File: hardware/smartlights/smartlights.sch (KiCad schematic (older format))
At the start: 9 parts, among them J1 Conn_02x20_Odd_Even_MountingP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, J2 Conn_01x02_MountingPin, J3 Conn_Coaxial_Power, Q1 IRLZ34N, U1 LM2596T-5

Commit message: Add switches to PCB, enlarging it.
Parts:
- added J10, J11, J4, J6, J7, J8, J9: Conn_01x02_MountingPin, Connector_PinHeader_2.54mm:PinHeader_1x02_P2.54mm_Vertical, symbol Connector_Generic:Conn_01x02
- added J5: Conn_01x04, Connector_PinHeader_2.54mm:PinHeader_1x04_P2.54mm_Vertical, symbol Connector_Generic:Conn_01x04
- added Q2, Q3, Q4, Q5, Q6: IRLZ34N, Package_TO_SOT_THT:TO-220-3_Vertical, symbol Transistor_FET:IRLZ34N
- J1: symbol Connector_Generic_MountingPin:Conn_02x20_Odd_Even_MountingPin -> Connector_Generic:Conn_02x20_Odd_Even
- J2: symbol Connector_Generic_MountingPin:Conn_01x02_MountingPin -> Connector_Generic:Conn_01x02
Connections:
- net labels added: 12V, 5V, 5V_raw, Data_19, Data_21, Data_7, Data_B, Data_G, Data_R, PWR,21, PWR_19, PWR_7, PWR_B, PWR_G, PWR_R
- wire segments 43 -> 70
- no-connect marks 39 -> 27
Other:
- moved on the sheet: C1, C2, D1, J3, L1, Q1, U1

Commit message: Neaten up labels, GND area
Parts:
- renumbered J2 to J1, J3 to J10, J1 to J11, J5 to J2, J6 to J3, J9 to J5, J8 to J6, J11 to J8, J10 to J9
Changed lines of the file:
@@
 $EndComp
 $Comp
-L Connector_Generic:Conn_01x04 J5
+L Connector_Generic:Conn_01x04 J2
 U 1 1 5E66A677
 P 900 4250
-F 0 "J5" V 864 3962 50  0000 R CNN
+F 0 "J2" V 864 3962 50  0000 R CNN
 F 1 "Conn_01x04" V 773 3962 50  0000 R CNN
 F 2 "Connector_PinHeader_2.54mm:PinHeader_1x04_P2.54mm_Vertical" H 900 4250 50  0001 C CNN
@@
 	1450 4150 1100 4150
 $Comp
-L Connector_Generic:Conn_01x02 J6
+L Connector_Generic:Conn_01x02 J3
 U 1 1 5E67B518
 P 1400 3550
-F 0 "J6" V 1364 3362 50  0000 R CNN
+F 0 "J3" V 1364 3362 50  0000 R CNN
 F 1 "Conn_01x02_MountingPin" V 1273 3362 50  0000 R CNN
 F 2 "Connector_PinHeader_2.54mm:PinHeader_1x02_P2.54mm_Vertical" H 1400 3550 50  0001 C CNN
@@
 	7800 3200 8400 3200
 $Comp
-L Connector:Conn_Coaxial_Power J3
+L Connector:Conn_Coaxial_Power J10
 U 1 1 5E60BF44
 P 5450 2700
-F 0 "J3" V 5233 2650 50  0000 C CNN
+F 0 "J10" V 5233 2650 50  0000 C CNN
 F 1 "Conn_Coaxial_Power" V 5324 2650 50  0000 C CNN
 F 2 "Connector_BarrelJack:BarrelJack_Horizontal" H 5450 2650 50  0001 C CNN
@@
 5V
 $Comp
-L Connector_Generic:Conn_01x02 J2
+L Connector_Generic:Conn_01x02 J1
 U 1 1 5E6126E2
 P 1400 5900
-F 0 "J2" V 1364 5712 50  0000 R CNN
+F 0 "J1" V 1364 5712 50  0000 R CNN
 F 1 "Conn_01x02_MountingPin" V 1273 5712 50  0000 R CNN
 F 2 "Connector_PinHeader_2.54mm:PinHeader_1x02_P2.54mm_Vertical" H 1400 5900 50  0001 C CNN
@@
 5V_raw
 $Comp
-L Connector_Generic:Conn_02x20_Odd_Even J1
+L Connector_Generic:Conn_02x20_Odd_Even J11
 U 1 1 5E600282
 P 3600 3450
-F 0 "J1" H 3650 4567 50  0000 C CNN
+F 0 "J11" H 3650 4567 50  0000 C CNN
 F 1 "Conn_02x20_Odd_Even_MountingPin" H 3650 4476 50  0000 C CNN
 F 2 "Connector_PinSocket_2.54mm:PinSocket_2x20_P2.54mm_Vertical" H 3600 3450 50  0001 C CNN
@@
 $EndComp
 $Comp
-L Connector_Generic:Conn_01x02 J8
+L Connector_Generic:Conn_01x02 J6
 U 1 1 5E7C76E0
 P 4650 3600
-F 0 "J8" V 4614 3412 50  0000 R CNN
+F 0 "J6" V 4614 3412 50  0000 R CNN
 F 1 "Conn_01x02_MountingPin" V 4523 3412 50  0000 R CNN
 F 2 "Connector_PinHeader_2.54mm:PinHeader_1x02_P2.54mm_Vertical" H 4650 3600 50  0001 C CNN
@@
 $EndComp
 $Comp
-L Connector_Generic:Conn_01x02 J9
+L Connector_Generic:Conn_01x02 J5
 U 1 1 5E7C7DFD
 P 4650 3850
-F 0 "J9" V 4614 3662 50  0000 R CNN
+F 0 "J5" V 4614 3662 50  0000 R CNN
 F 1 "Conn_01x02_MountingPin" V 4523 3662 50  0000 R CNN
 F 2 "Connector_PinHeader_2.54mm:PinHeader_1x02_P2.54mm_Vertical" H 4650 3850 50  0001 C CNN
@@
 Wire Wire Line
 	4450 3350 3900 3350
-Wire Wire Line
-	4450 3600 4200 3600
-Wire Wire Line
-	4200 3600 4200 3550
-Wire Wire Line
-	4200 3550 3900 3550
-Wire Wire Line
-	4450 3850 4100 3850
-Wire Wire Line
-	4100 3850 4100 3650
-Wire Wire Line
-	4100 3650 3900 3650
-$Comp
-L Connector_Generic:Conn_01x02 J11
+$Comp
+L Connector_Generic:Conn_01x02 J8
 U 1 1 5E7E2973
 P 4650 3100
-F 0 "J11" V 4614 2912 50  0000 R CNN
+F 0 "J8" V 4614 2912 50  0000 R CNN
 F 1 "Conn_01x02_MountingPin" V 4523 2912 50  0000 R CNN
 F 2 "Connector_PinHeader_2.54mm:PinHeader_1x02_P2.54mm_Vertical" H 4650 3100 50  0001 C CNN
@@
 $EndComp
 $Comp
-L Connector_Generic:Conn_01x02 J10
+L Connector_Generic:Conn_01x02 J9
 U 1 1 5E7E2D89
 P 4650 2850
-F 0 "J10" V 4614 2662 50  0000 R CNN
+F 0 "J9" V 4614 2662 50  0000 R CNN
 F 1 "Conn_01x02_MountingPin" V 4523 2662 50  0000 R CNN
 F 2 "Connector_PinHeader_2.54mm:PinHeader_1x02_P2.54mm_Vertical" H 4650 2850 50  0001 C CNN
@@
 	1    0    0    -1
 $EndComp
-Wire Wire Line
-	4450 3100 4200 3100
-Wire Wire Line
-	4200 3100 4200 3250
-Wire Wire Line
-	4200 3250 3900 3250
-Wire Wire Line
-	3900 3150 4100 3150
-Wire Wire Line
-	4100 3150 4100 2850
-Wire Wire Line
-	4100 2850 4450 2850
 Text GLabel 4450 2950 0    50   Input ~ 0
 GND
@@
 Text GLabel 4450 3950 0    50   Input ~ 0
 GND
+Wire Wire Line
+	4100 3150 4100 2850
+Wire Wire Line
+	3900 3150 4100 3150
+Wire Wire Line
+	4100 2850 4450 2850
+Wire Wire Line
+	4200 3100 4200 3250
+Wire Wire Line
+	4450 3100 4200 3100
+Wire Wire Line
+	4200 3250 3900 3250
+Wire Wire Line
+	4100 3850 4100 3650
+Wire Wire Line
+	4450 3850 4100 3850
+Wire Wire Line
+	4100 3650 3900 3650
+Wire Wire Line
+	4200 3550 3900 3550
+Wire Wire Line
+	4450 3600 4200 3600
+Wire Wire Line
+	4200 3600 4200 3550
 $EndSCHEMATC

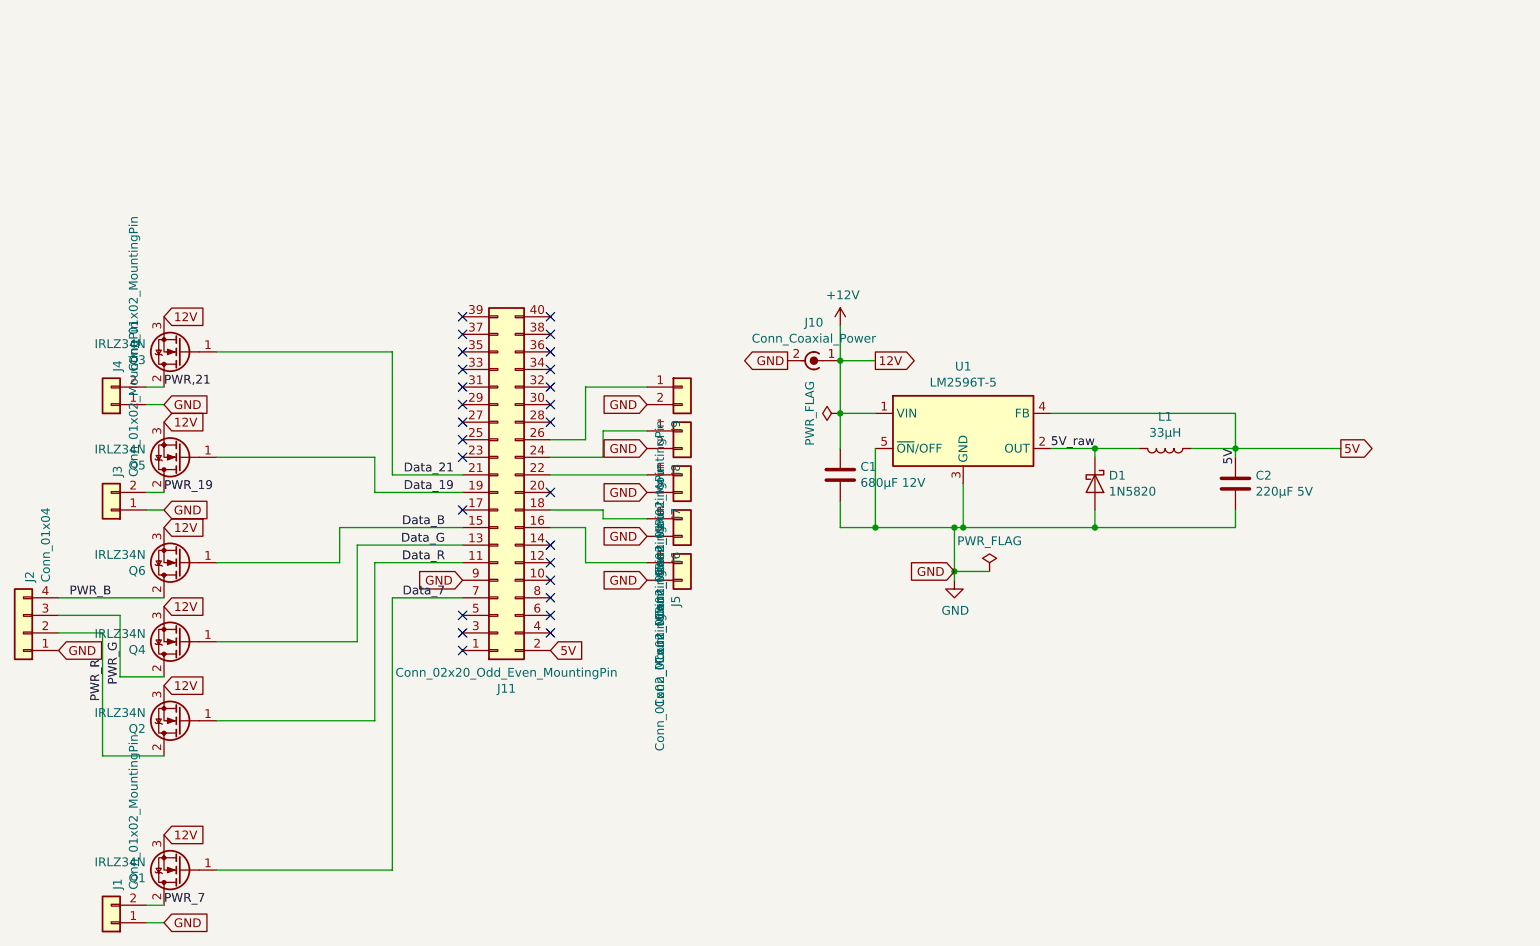
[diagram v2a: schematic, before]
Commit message: PCB: Use RasPi footprint, reduce GND area around jacks
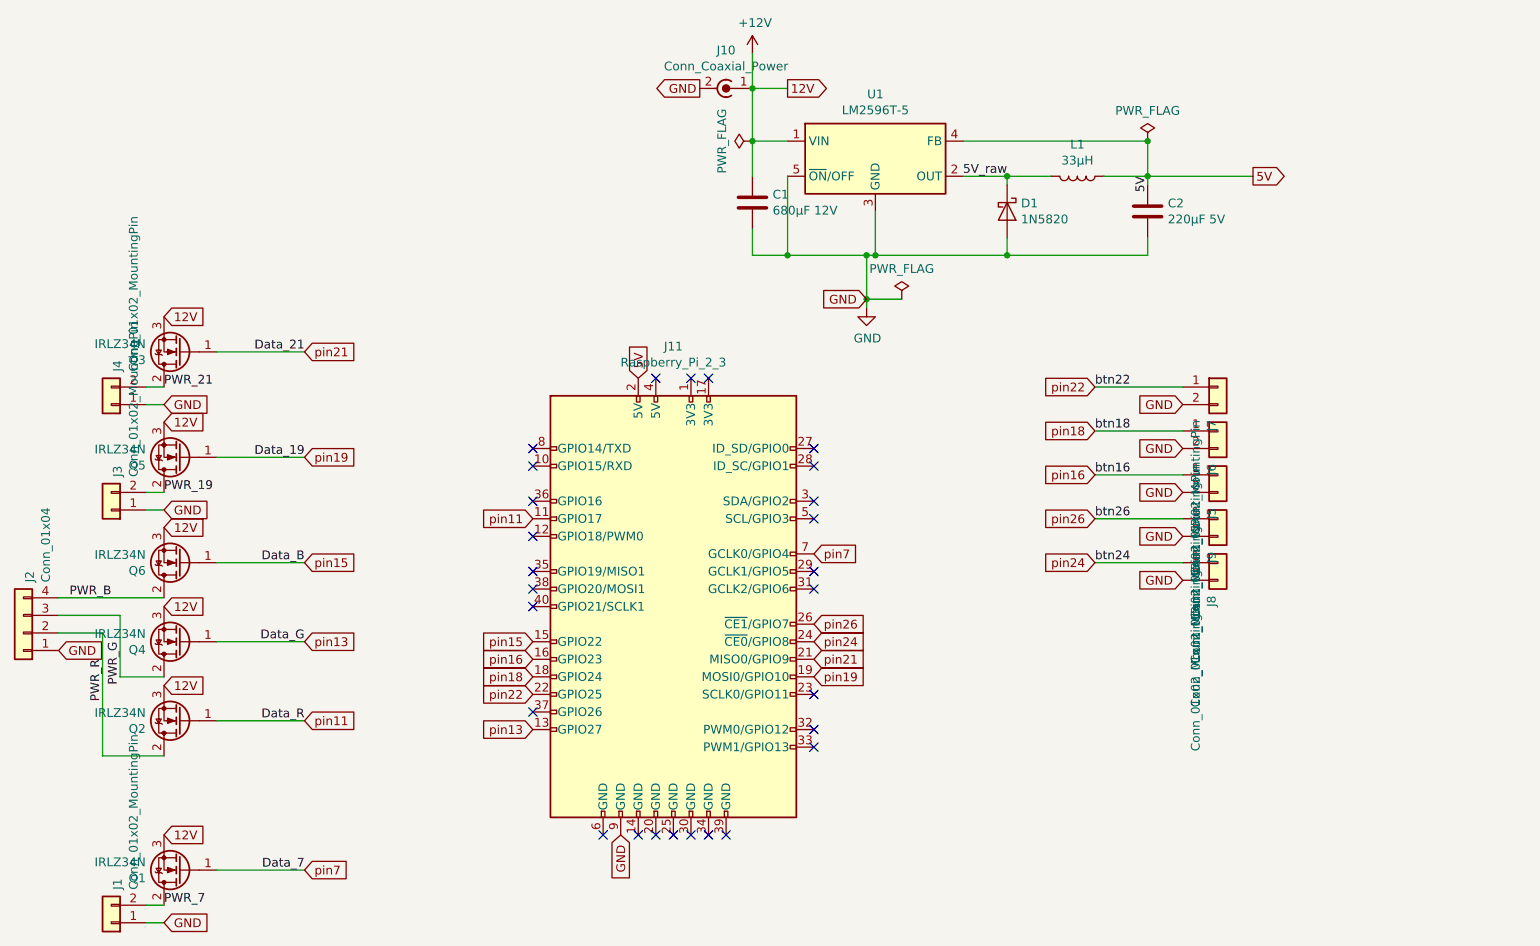
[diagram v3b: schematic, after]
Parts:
- removed J11: Conn_02x20_Odd_Even_MountingPin, Connector_PinSocket_2.54mm:PinSocket_2x20_P2.54mm_Vertical, symbol Connector_Generic:Conn_02x20_Odd_Even
- added J11: Raspberry_Pi_2_3, Module:Raspberry_Pi_Zero_Socketed_THT_FaceDown_MountingHoles, symbol Connector:Raspberry_Pi_2_3
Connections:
- net 5V: now also J11.2 (5V)
- net GND: now also J11.9 (GND)
- net pin16: now reaches J5.1 (Pin_1)
- net pin16: now also J11.16 (GPIO23)
- net pin18: now reaches J6.1 (Pin_1)
- net pin18: now also J11.18 (GPIO24)
- net pin22: now reaches J7.1 (Pin_1)
- net pin22: now also J11.22 (GPIO25)
- net pin24: now reaches J8.1 (Pin_1)
- net pin24: now also J11.24 (~CE0~/GPIO8)
- net pin26: now reaches J9.1 (Pin_1)
- net pin26: now also J11.26 (~CE1~/GPIO7)
- net Data_19 renamed pin19
- net pin19: now also J11.19 (MOSI0/GPIO10)
- net Data_21 renamed pin21
- net pin21: now also J11.21 (MISO0/GPIO9)
- net Data_7 renamed pin7
- net pin7: now also J11.7 (GCLK0/GPIO4)
- net Data_B renamed pin15
- net pin15: now also J11.15 (GPIO22)
- net Data_G renamed pin13
- net pin13: now also J11.13 (GPIO27)
- net Data_R renamed pin11
- net pin11: now also J11.11 (GPIO17)
- net PWR,21 renamed PWR_21
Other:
- moved on the sheet: C1, C2, D1, J10, J5, J6, J7, J8, J9, L1, U1

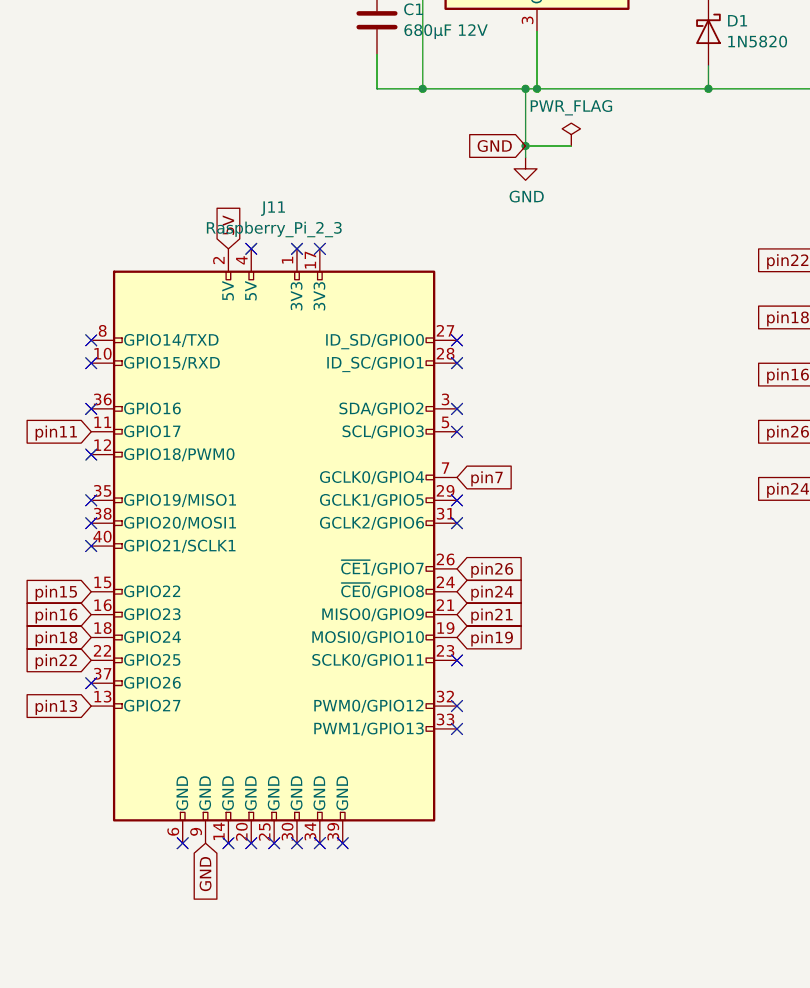
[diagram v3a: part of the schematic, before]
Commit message: Add power button and connect more 5V/GND pins. For beaut.
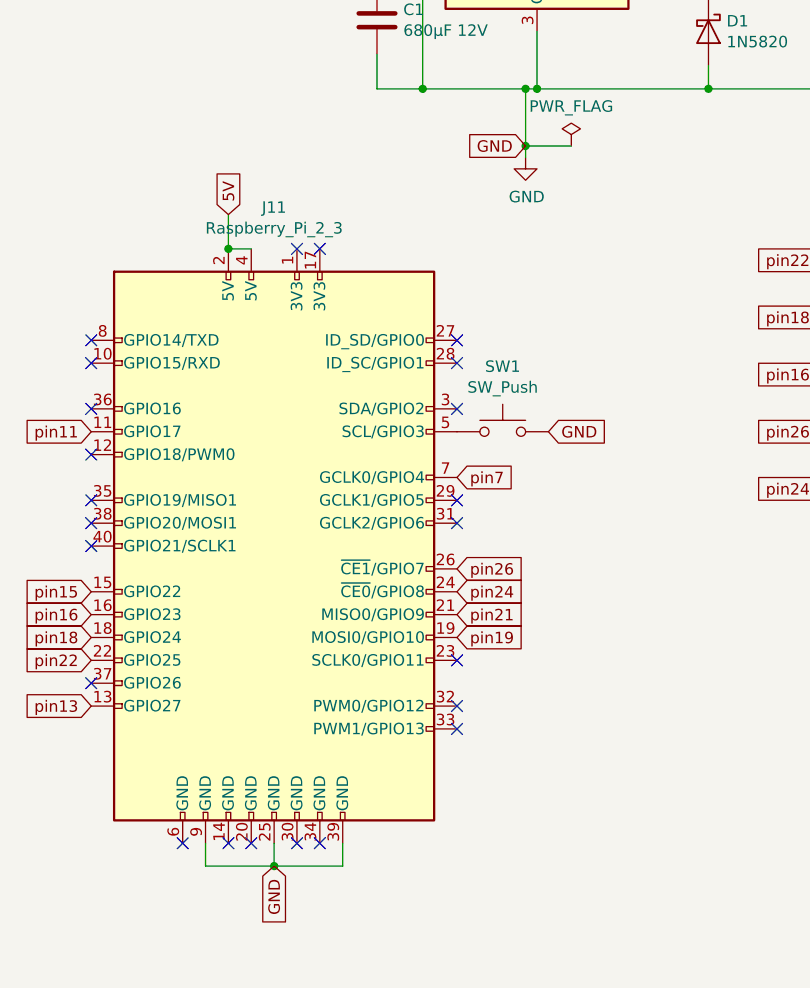
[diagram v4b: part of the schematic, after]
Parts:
- added SW1: SW_Push, Button_Switch_THT:SW_PUSH_6mm, symbol Switch:SW_Push
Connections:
- net 5V: now also J11.4 (5V)
- net GND: now also J11.25 (GND), J11.39 (GND), SW1.2
- net at J11.5 (SCL/GPIO3): now also SW1.1
- no-connect marks 27 -> 23
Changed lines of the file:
@@
 	1    0    0    -1
 $EndComp
-Text GLabel 4400 2800 1    50   Input ~ 0
+Text GLabel 4400 2650 1    50   Input ~ 0
 5V
 Text GLabel 5250 1150 2    50   Output ~ 0
@@
 Text GLabel 1700 3550 2    50   Input ~ 0
 GND
-Text GLabel 4300 5400 3    50   Input ~ 0
+Text GLabel 4600 5500 3    50   Input ~ 0
 GND
 Wire Wire Line
@@
 NoConn ~ 5400 3300
 NoConn ~ 5400 3200
-NoConn ~ 4900 5400
-NoConn ~ 4800 5400
 Text GLabel 5400 3800 2    50   Input ~ 0
 pin7
@@
 NoConn ~ 3800 4100
 NoConn ~ 5400 3500
-NoConn ~ 5400 3600
 NoConn ~ 5400 4600
 NoConn ~ 5400 4800
 NoConn ~ 5400 4900
-NoConn ~ 4200 5400
-NoConn ~ 4400 5400
-NoConn ~ 4500 5400
-NoConn ~ 4600 5400
-NoConn ~ 4700 5400
-NoConn ~ 4500 2800
 NoConn ~ 4700 2800
 NoConn ~ 4800 2800
@@
 $EndComp
 Connection ~ 7300 1450
+Wire Wire Line
+	4500 2800 4400 2800
+Wire Wire Line
+	4400 2800 4400 2650
+Connection ~ 4400 2800
+Wire Wire Line
+	4900 5400 4900 5500
+Wire Wire Line
+	4900 5500 4600 5500
+Wire Wire Line
+	4600 5500 4600 5400
+NoConn ~ 4700 5400
+NoConn ~ 4800 5400
+$Comp
+L Switch:SW_Push SW1
+U 1 1 5E7FD75B
+P 5600 3600
+F 0 "SW1" H 5600 3885 50  0000 C CNN
+F 1 "SW_Push" H 5600 3794 50  0000 C CNN
+F 2 "Button_Switch_THT:SW_PUSH_6mm" H 5600 3800 50  0001 C CNN
+F 3 "~" H 5600 3800 50  0001 C CNN
+	1    5600 3600
+	1    0    0    -1
+$EndComp
+Text GLabel 5800 3600 2    50   Input ~ 0
+GND
+NoConn ~ 4200 5400
+NoConn ~ 4400 5400
+NoConn ~ 4500 5400
+Wire Wire Line
+	4600 5500 4300 5500
+Wire Wire Line
+	4300 5500 4300 5400
+Connection ~ 4600 5500
 $EndSCHEMATC
